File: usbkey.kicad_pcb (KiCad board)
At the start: 2 copper layers, 13 x 11 mm, 16 parts, among them P1 USART0, P2 DEBUG, P3 USB_B, U1 EFM32HG309

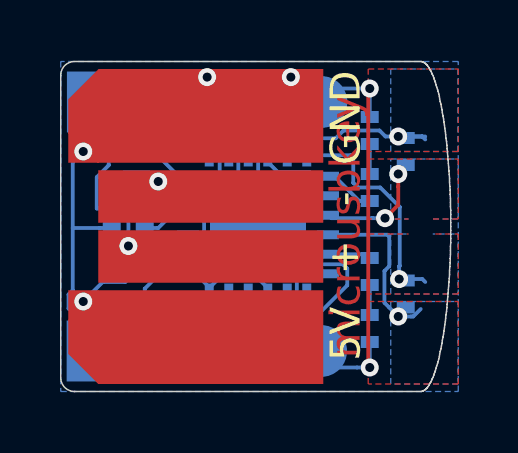
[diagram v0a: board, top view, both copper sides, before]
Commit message: Fixing the D+/D- direction.
 * Still need to fix the board routing...
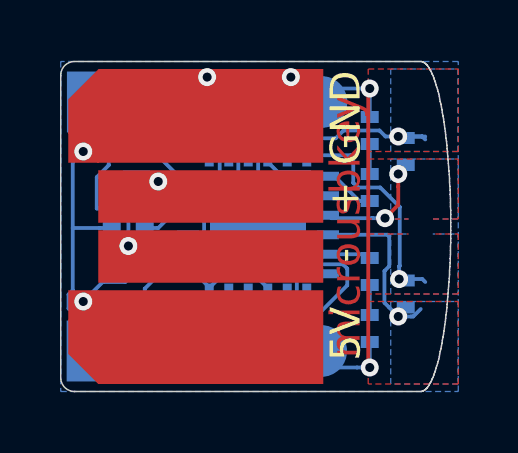
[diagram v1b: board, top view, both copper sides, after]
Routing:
- net /USB_D-: track 4.04 -> 4.97 mm
- net /USB_D+: track 6.99 -> 6.05 mm
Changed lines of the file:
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@@
-(kicad_pcb (version 4) (host pcbnew 4.0.2+e4-6225~38~ubuntu14.04.1-stable)
+(kicad_pcb (version 4) (host pcbnew 4.1.0-alpha+201606170817+6938~45~ubuntu14.04.1-product)
   (general
     (links 42)
-    (no_connects 0)
-    (area -14.106763 -3.052 139.257141 44.375)
+    (no_connects 2)
+    (area -14.106762 -2.8845 139.407143 45.245)
     (thickness 1.6)
     (drawings 174)
@@
       (hpglpenspeed 20)
       (hpglpendiameter 15)
-      (hpglpenoverlay 2)
       (psnegative false)
       (psa4output false)
@@
     (tags "LED led 0402 SMD smd SMT smt smdled SMDLED smtled SMTLED")
     (attr smd)
-    (fp_text reference D2 (at 0.1 1.325 360) (layer B.SilkS) hide
+    (fp_text reference D2 (at 0.1 1.325) (layer B.SilkS) hide
       (effects (font (size 0.6 0.6) (thickness 0.15)) (justify mirror))
     )
@@
       (effects (font (size 1 1) (thickness 0.15)))
     )
-    (fp_text user + (at 9.45 -4.475 90) (layer F.SilkS)
+    (fp_text user + (at 9.46 -6.43 90) (layer F.SilkS)
       (effects (font (size 1 1) (thickness 0.15)))
     )
@@
     (fp_poly (pts (xy 8.5 -10.25) (xy 8.5 -7.75) (xy 0.75 -7.75) (xy 0.75 -9.75)
       (xy 1.25 -10.25) (xy 8.5 -10.25)) (layer F.Mask) (width 0.01))
-    (fp_text user - (at 9.45 -6.425 90) (layer F.SilkS)
+    (fp_text user - (at 9.44 -4.54 90) (layer F.SilkS)
       (effects (font (size 1 1) (thickness 0.15)))
     )
@@
     (pad 4 connect rect (at 5 -9.1875) (size 7.5 3.125) (layers F.Cu)
       (net 1 GND) (zone_connect 2))
-    (pad 3 connect rect (at 5 -4.5) (size 7.5 1.75) (layers F.Cu)
+    (pad 2 connect rect (at 5 -4.5) (size 7.5 1.75) (layers F.Cu)
+      (net 9 /USB_D-) (zone_connect 2))
+    (pad 3 connect rect (at 5 -6.5) (size 7.5 1.75) (layers F.Cu)
       (net 8 /USB_D+) (zone_connect 2))
-    (pad 2 connect rect (at 5 -6.5) (size 7.5 1.75) (layers F.Cu)
-      (net 9 /USB_D-) (zone_connect 2))
     (pad 1 connect trapezoid (at 0.75 -1.8125 180) (size 1 2.125) (rect_delta 1 0 ) (layers F.Cu)
       (net 3 /USB_5V) (zone_connect 2))
@@
   (segment (start 18.873602 22.9) (end 19.255382 23.28178) (width 0.127) (layer B.Cu) (net 8))
   (segment (start 19.255382 23.28178) (end 19.255382 24.150004) (width 0.127) (layer B.Cu) (net 8))
-  (segment (start 19.555381 24.450003) (end 19.255382 24.150004) (width 0.127) (layer F.Cu) (net 8))
-  (segment (start 19.60538 24.5) (end 19.555381 24.450003) (width 0.127) (layer F.Cu) (net 8))
-  (segment (start 22 24.5) (end 19.60538 24.5) (width 0.127) (layer F.Cu) (net 8))
-  (via (at 19.255382 24.150004) (size 0.6) (drill 0.3) (layers F.Cu B.Cu) (net 8))
+  (segment (start 20.549999 22.299985) (end 20.25 21.999986) (width 0.127) (layer F.Cu) (net 8))
+  (segment (start 22 22.5) (end 20.750014 22.5) (width 0.127) (layer F.Cu) (net 8))
+  (segment (start 20.750014 22.5) (end 20.549999 22.299985) (width 0.127) (layer F.Cu) (net 8))
+  (via (at 20.25 21.999986) (size 0.6) (drill 0.3) (layers F.Cu B.Cu) (net 8))
+  (segment (start 19.555381 24.450003) (end 19.255382 24.150004) (width 0.127) (layer F.Cu) (net 9))
+  (segment (start 19.60538 24.5) (end 19.555381 24.450003) (width 0.127) (layer F.Cu) (net 9))
+  (segment (start 22 24.5) (end 19.60538 24.5) (width 0.127) (layer F.Cu) (net 9))
+  (via (at 19.255382 24.150004) (size 0.6) (drill 0.3) (layers F.Cu B.Cu) (net 9))
   (segment (start 18.6 22.2) (end 19.100013 21.699987) (width 0.127) (layer B.Cu) (net 9))
   (segment (start 18.6 22.3) (end 18.6 22.2) (width 0.127) (layer B.Cu) (net 9))
-  (segment (start 20.549999 22.299985) (end 20.25 21.999986) (width 0.127) (layer F.Cu) (net 9))
-  (segment (start 22 22.5) (end 20.750014 22.5) (width 0.127) (layer F.Cu) (net 9))
-  (segment (start 20.750014 22.5) (end 20.549999 22.299985) (width 0.127) (layer F.Cu) (net 9))
   (segment (start 19.950001 21.699987) (end 20.25 21.999986) (width 0.127) (layer B.Cu) (net 9))
   (segment (start 19.100013 21.699987) (end 19.950001 21.699987) (width 0.127) (layer B.Cu) (net 9))
-  (via (at 20.25 21.999986) (size 0.6) (drill 0.3) (layers F.Cu B.Cu) (net 9))
   (segment (start 19.8 25.573) (end 19.8 25.95) (width 0.127) (layer B.Cu) (net 12))
   (segment (start 20.345989 24.744786) (end 20.345989 25.027011) (width 0.127) (layer B.Cu) (net 12))

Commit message: Lots of small fixes.
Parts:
- moved R3 0.45 mm to (19.5, 22.3)
- moved R4 0.45 mm to (19.5, 21.0)
- moved C1 0.07 mm to (19.3, 25.9)
- moved C2 0.07 mm to (19.3, 23.6)
- moved C3 0.07 mm to (19.3, 24.8)
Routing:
- net GND: track 41.2 -> 48.5 mm
- net /USB_D-: track 4.97 -> 7.43 mm
- net /RUSB_D-: track 1.99 -> 1.37 mm
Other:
- net class Default: clearance 0.127 -> 0.1016
- rule trace_clearance: 0.127 -> 0.1016
- board text removed: "microusbkey"
